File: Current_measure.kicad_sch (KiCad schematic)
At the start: 0 parts

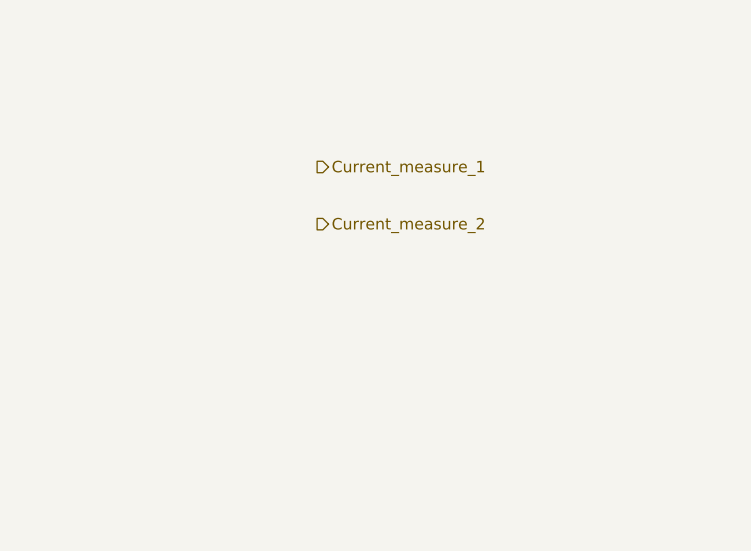
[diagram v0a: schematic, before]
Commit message: VER1.0: добавил защиту бортового питания для тестов по ISO 7637-2 (Степень III)
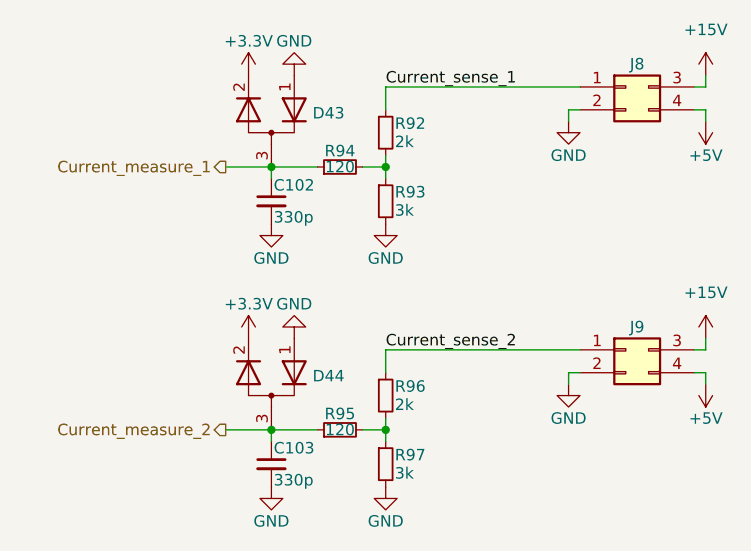
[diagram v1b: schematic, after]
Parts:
- added C102, C103: 330p, Capacitor_SMD:C_0805_2012Metric_Pad1.18x1.45mm_HandSolder, symbol Device:C_Small
- added D43, D44: (no value), Package_TO_SOT_SMD:SOT-23, symbol Device:D_Dual_Series_AKC_Parallel
- added J8, J9: (no value), symbol Connector_Generic:Conn_02x02_Top_Bottom
- added R92, R96: 2k, Resistor_SMD:R_0805_2012Metric_Pad1.20x1.40mm_HandSolder, symbol Device:R_Small
- added R93, R97: 3k, Resistor_SMD:R_0805_2012Metric_Pad1.20x1.40mm_HandSolder, symbol Device:R_Small
- added R94, R95: 120, Resistor_SMD:R_0805_2012Metric_Pad1.20x1.40mm_HandSolder, symbol Device:R_Small
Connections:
- net Current_measure_1: now also C102.1, D43.3 (common), R94.1
- net Current_measure_2: now also C103.1, D44.3 (common), R95.1
- new net: R92.2, R93.1, R94.2
- new net: R95.2, R96.2, R97.1
- new net +15V: J8.3 (Pin_3), J9.3 (Pin_3)
- new net +3.3V: D43.2 (K), D44.2 (K)
- new net +5V: J8.4 (Pin_4), J9.4 (Pin_4)
- new net Current_sense_1: J8.1 (Pin_1), R92.1
- new net Current_sense_2: J9.1 (Pin_1), R96.1
- new net GND: C102.2, C103.2, D43.1 (A), D44.1 (A), J8.2 (Pin_2), J9.2 (Pin_2), R93.2, R97.2

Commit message: VER1.0: добавил разъемы для платы вторички
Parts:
- removed J8, J9: (no value), symbol Connector_Generic:Conn_02x02_Top_Bottom
- added J8, J9: (no value), Connector_Molex:Molex_Mini-Fit_Jr_5569-06A2_2x03_P4.20mm_Horizontal, symbol Connector_Generic:Conn_02x03_Odd_Even
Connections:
- net +15V: now also J8.2 (Pin_2), J9.2 (Pin_2)
- net +5V: now also J8.3 (Pin_3), J9.3 (Pin_3)
- net Current_sense_1: now also J8.1 (Pin_1)
- net Current_sense_2: now also J9.1 (Pin_1)
- net GND: now also J8.4 (Pin_4), J8.5 (Pin_5), J8.6 (Pin_6), J9.4 (Pin_4), J9.5 (Pin_5), J9.6 (Pin_6)

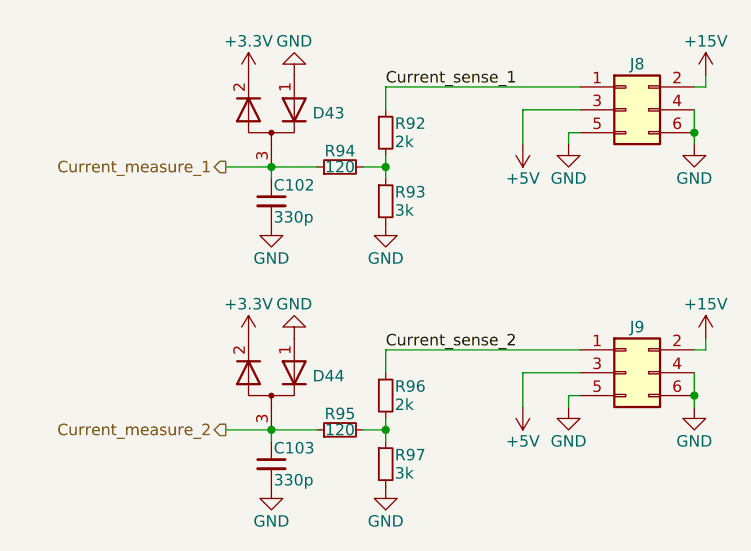
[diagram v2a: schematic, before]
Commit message: VER1.0: добавил разделение питания VDD и VDDA
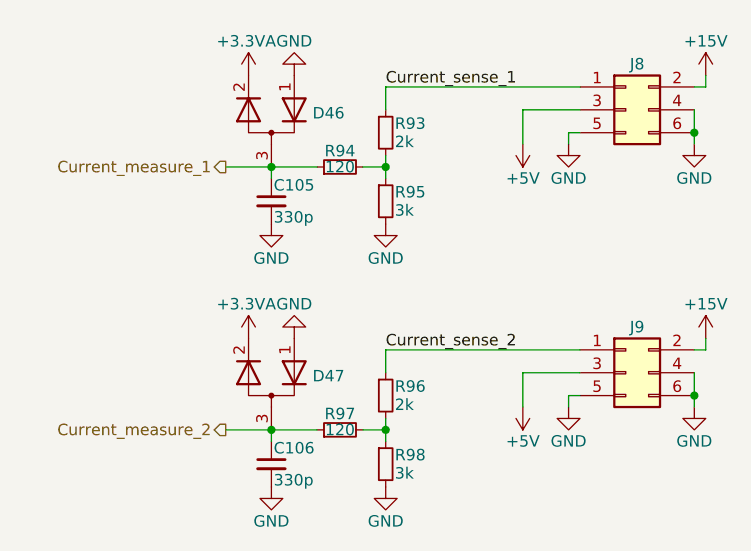
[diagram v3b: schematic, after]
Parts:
- C105: renamed from C102; Description P/N (none) -> Capacitor SMD 25V
- C106: renamed from C103; Description P/N (none) -> Capacitor SMD 25V
- J8, J9: Description P/N (none) -> Connector; Product Name (none) -> DS1073-01-2x3MR2T6
- R93: renamed from R92; Description P/N (none) -> Resistor SMD 0.1%; Product Name RT0805BRD072KL -> (none)
- R94: Description P/N (none) -> Resistor SMD 1%
- R95: renamed from R93; Description P/N (none) -> Resistor SMD 0.1%; Product Name RT0805BRD073KL -> (none)
- R96: Description P/N (none) -> Resistor SMD 0.1%; Product Name RT0805BRD072KL -> (none)
- R97: renamed from R95; Description P/N (none) -> Resistor SMD 1%
- R98: renamed from R97; Description P/N (none) -> Resistor SMD 0.1%; Product Name RT0805BRD073KL -> (none)
- renumbered D43 to D46, D44 to D47
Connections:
- net +3.3V renamed +3.3VA
